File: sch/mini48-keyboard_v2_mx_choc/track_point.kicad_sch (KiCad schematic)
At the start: 22 parts, among them J1 Conn_01x08, Q1 BSS138, Q2 BSS138, Q3 BSS138, SW100 SW_Push, SW101 SW_Push, SW102 SW_Push, SW97 SW_Push, SW98 SW_Push, SW99 SW_Push

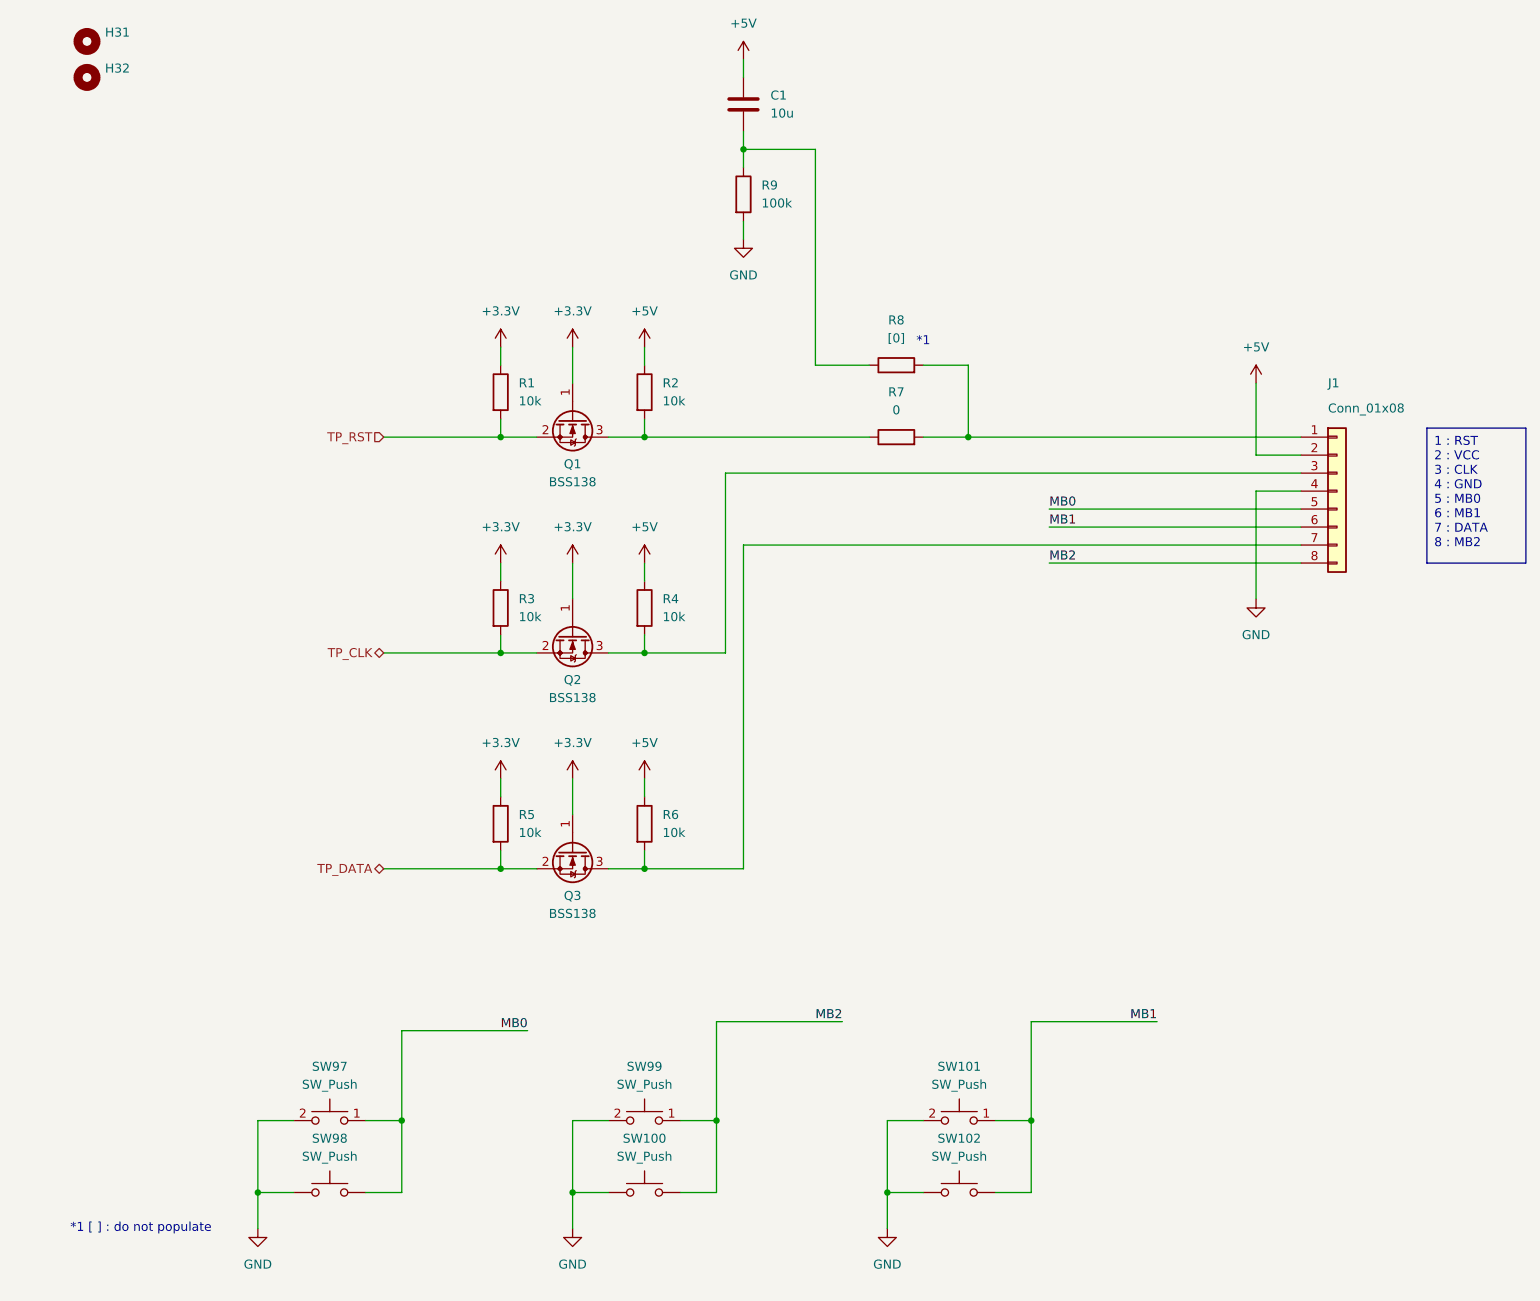
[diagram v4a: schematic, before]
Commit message: picoの位置を左上に変更しました。
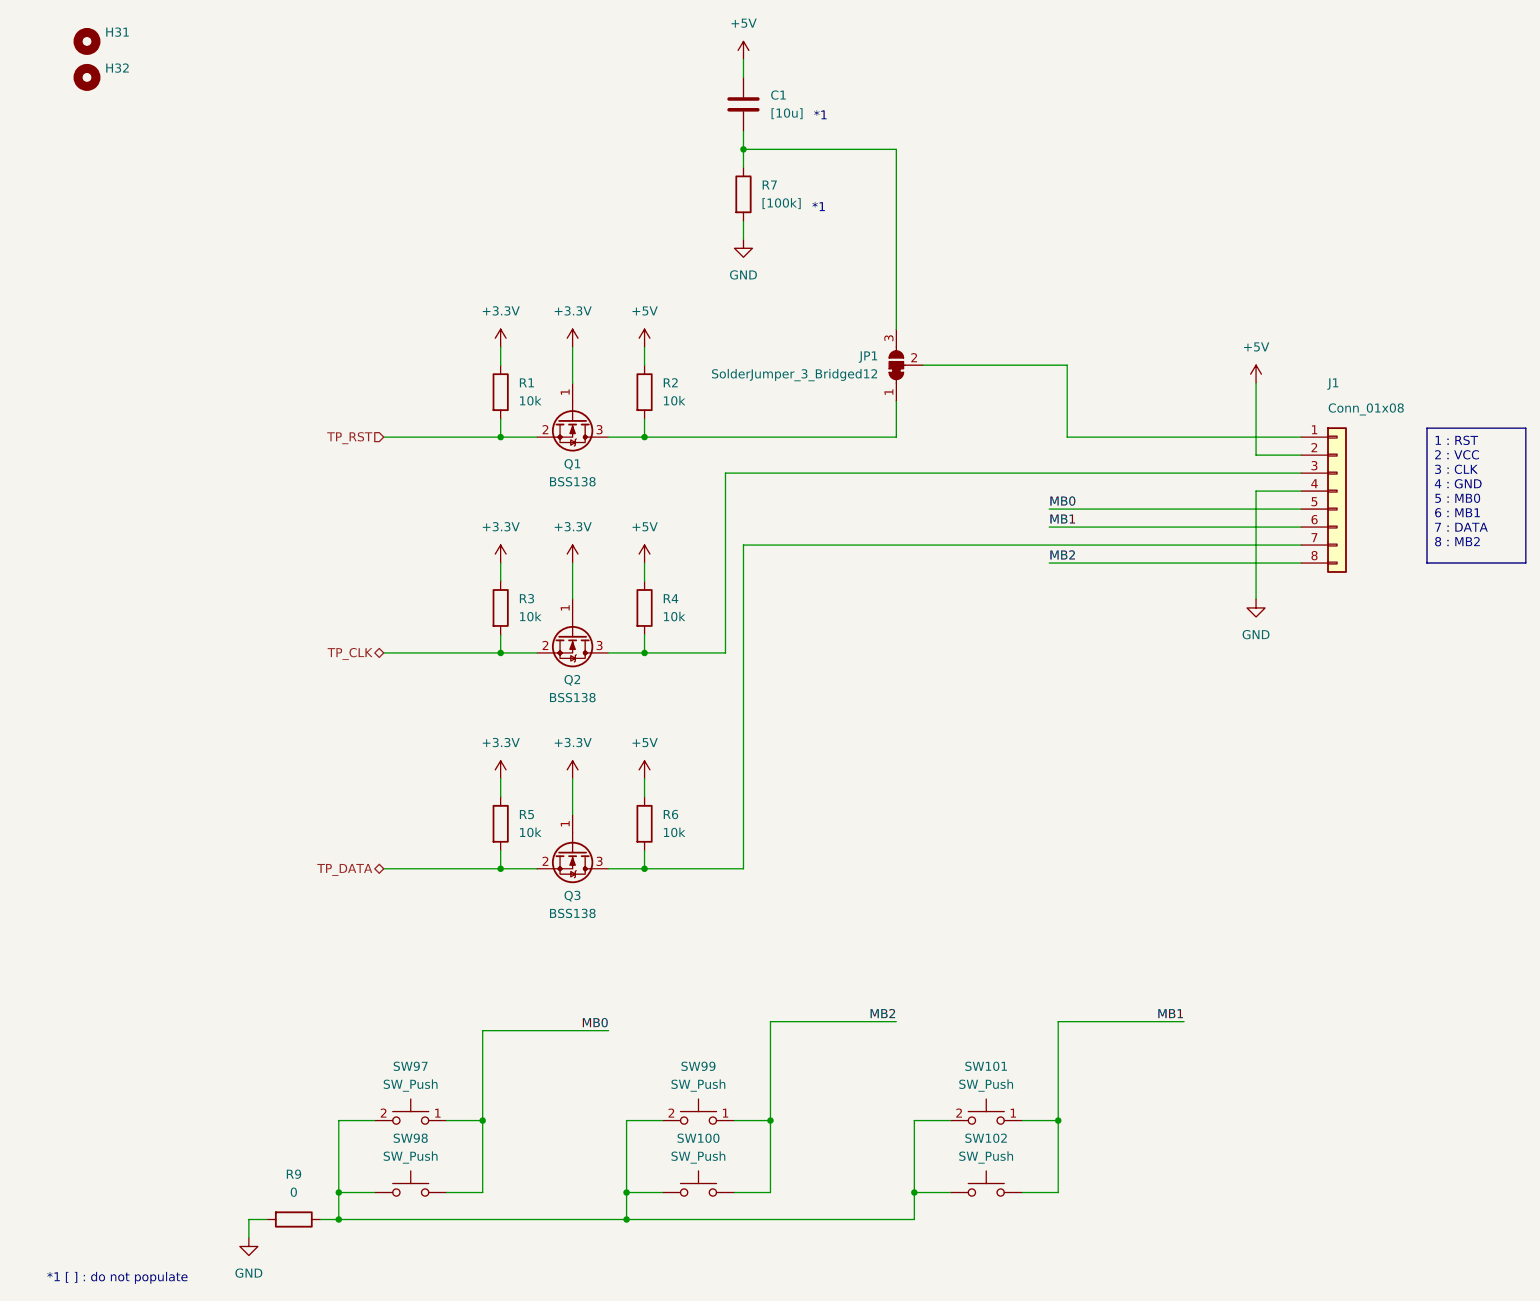
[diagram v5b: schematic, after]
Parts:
- removed R7: 0, Resistor_SMD:R_0603_1608Metric, symbol Device:R
- removed R8: [0], Resistor_SMD:R_0603_1608Metric, symbol Device:R
- added JP1: SolderJumper_3_Bridged12, Jumper:SolderJumper-3_P1.3mm_Bridged12_RoundedPad1.0x1.5mm, symbol Jumper:SolderJumper_3_Bridged12
- added R9: 0, Resistor_SMD:R_0603_1608Metric, symbol Device:R
- C1: value 10u -> [10u]
- J1: footprint Connector_JST:JST_XH_S8B-XH-A_1x08_P2.50mm_Horizontal -> Connector_JST:JST_PH_B8B-PH-K_1x08_P2.00mm_Vertical
- R7: renamed from R9; value 100k -> [100k]
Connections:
- net GND: now also R9.2; no longer SW100.1, SW101.2, SW102.1, SW97.2, SW98.1, SW99.2
- net at C1.2, R7.1: now also JP1.3 (B)
- net at Q1.3 (D), R2.2: now also JP1.1 (A)
- net at J1.1 (Pin_1): now also JP1.2 (C)
- new net: R9.1, SW100.1, SW101.2, SW102.1, SW97.2, SW98.1, SW99.2
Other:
- moved on the sheet: SW100, SW101, SW102, SW97, SW98, SW99
